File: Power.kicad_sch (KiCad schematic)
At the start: 74 parts, among them J100 CON-SOCJ-2155, Q100 T2N7002AK,LM, U100 LS1205EVD33, U101 SY8003ADFC, U102 SY8003ADFC, U103 SY8003ADFC, U104 SY8003ADFC, U105 BD3539FVM

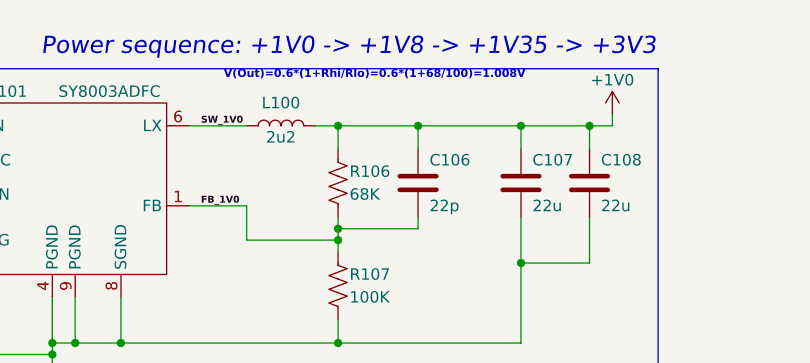
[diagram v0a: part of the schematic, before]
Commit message: Schematic page 2 done, Zynq Power
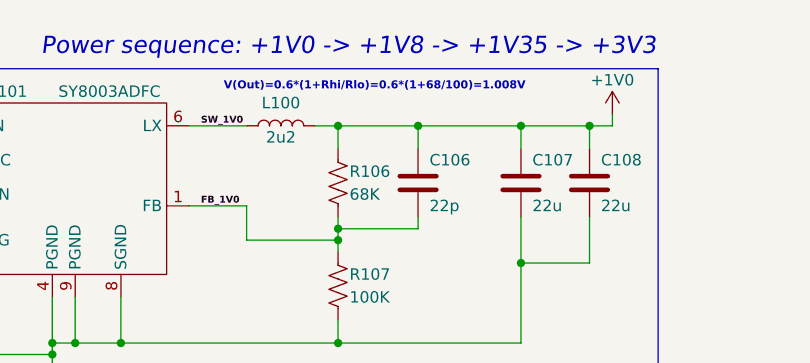
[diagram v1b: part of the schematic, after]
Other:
- title: ZeBra-X: A Xylinx Zynq Demo Board -> ZeBra-X: A Xilinx Zynq Demo Board
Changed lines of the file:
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@@
   (paper "A4")
   (title_block
-    (title "ZeBra-X: A Xylinx Zynq Demo Board")
+    (title "ZeBra-X: A Xilinx Zynq Demo Board")
     (date "2023-12-09")
     (rev "-")
@@
     (effects (font (size 1.27 1.27) bold) (justify left bottom))
   )
-  (text "V(Out)=0.6*(1+Rhi/Rlo)=0.6*(1+68/100)=1.008V" (at 234.95 20.32 0)
+  (text "V(Out)=0.6*(1+Rhi/Rlo)=0.6*(1+68/100)=1.008V" (at 234.95 21.59 0)
     (effects (font (size 0.889 0.889) bold) (justify left bottom))
   )

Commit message: Fixed Q100 footprint
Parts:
- Q100: footprint Package_TO_SOT_SMD:SOT-23 -> ZeBra_footprints:SOT23_TOS; symbol Simulation_SPICE:NMOS -> ZeBra-X:NMOS_T2N7002AKLM
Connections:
- net GND: now also Q100.2 (S); no longer Q100.3 (S)
- net LED_PWR_K: now also Q100.3 (D); no longer Q100.1 (D)
- net at R124.1: now also Q100.1 (G); no longer Q100.2 (G)
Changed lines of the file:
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@@
     )
   )
-  (symbol (lib_id "Simulation_SPICE:NMOS") (at 138.43 185.42 0) (unit 1)
+  (symbol (lib_id "ZeBra-X:NMOS_T2N7002AKLM") (at 138.43 185.42 0) (unit 1)
     (in_bom yes) (on_board yes) (dnp no)
     (property "Reference" "Q100" (at 132.08 189.23 0)
@@
       (effects (font (size 1.27 1.27)) (justify left))
     )
-    (property "Footprint" "Package_TO_SOT_SMD:SOT-23" (at 143.51 182.88 0)
+    (property "Footprint" "ZeBra_footprints:SOT23_TOS" (at 143.51 182.88 0)
       (effects (font (size 1.27 1.27)) hide)
     )

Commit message: Finished page 3 of schematic: Zynq Config, JTAG, Debug
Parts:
- R128: Distributor Link (none) -> -; LCSC PN (none) -> -; Manufacturer (none) -> -; Manufacturer PN (none) -> -
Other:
- title: ZeBra-X: A Xilinx Zynq Demo Board -> Power Supplies
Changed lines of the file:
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@@
   (paper "A4")
   (title_block
-    (title "ZeBra-X: A Xilinx Zynq Demo Board")
+    (title "Power Supplies")
     (date "2023-12-09")
     (rev "-")
@@
       (effects (font (size 1.27 1.27)) hide)
     )
-    (property "Datasheet" "" (at 35.56 176.53 0)
+    (property "Datasheet" "-" (at 35.56 176.53 0)
       (effects (font (size 1.27 1.27)) hide)
     )
-    (property "Description" "" (at 35.56 176.53 0)
+    (property "Description" "-" (at 35.56 176.53 0)
       (effects (font (size 1.27 1.27)) hide)
     )
-    (property "Distributor Link" "" (at 35.56 176.53 0)
+    (property "Distributor Link" "-" (at 35.56 176.53 0)
       (effects (font (size 1.27 1.27)) hide)
     )
-    (property "LCSC PN" "" (at 35.56 176.53 0)
+    (property "LCSC PN" "-" (at 35.56 176.53 0)
       (effects (font (size 1.27 1.27)) hide)
     )
-    (property "Manufacturer" "" (at 35.56 176.53 0)
+    (property "Manufacturer" "-" (at 35.56 176.53 0)
       (effects (font (size 1.27 1.27)) hide)
     )
-    (property "Manufacturer PN" "" (at 35.56 176.53 0)
+    (property "Manufacturer PN" "-" (at 35.56 176.53 0)
       (effects (font (size 1.27 1.27)) hide)
     )

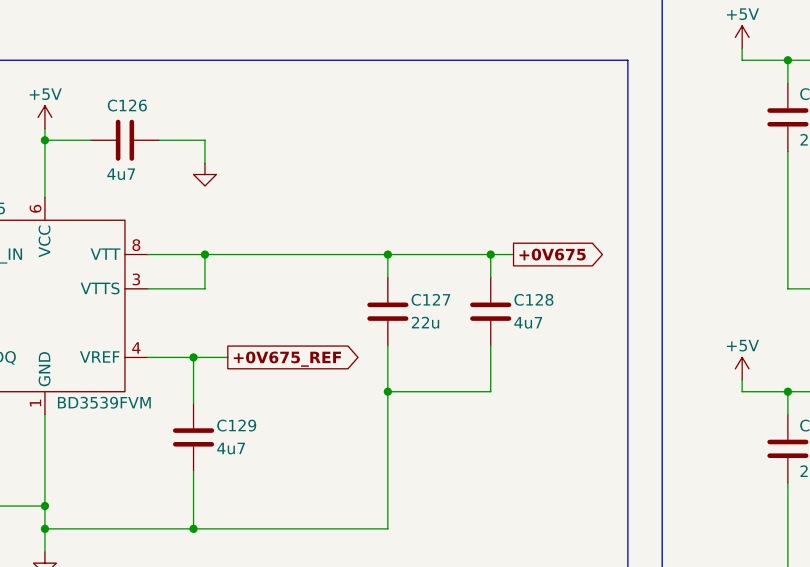
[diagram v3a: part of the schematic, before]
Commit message: Added page '[7] 1GB DDR3L Modules'
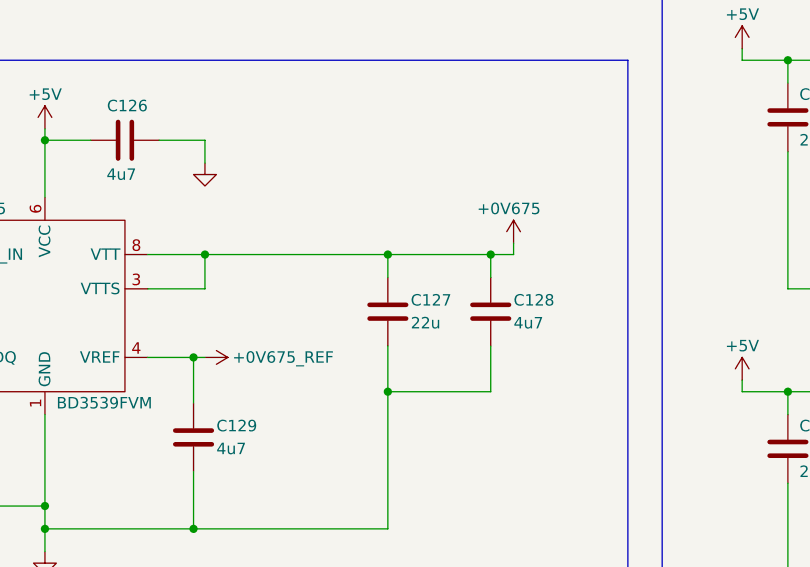
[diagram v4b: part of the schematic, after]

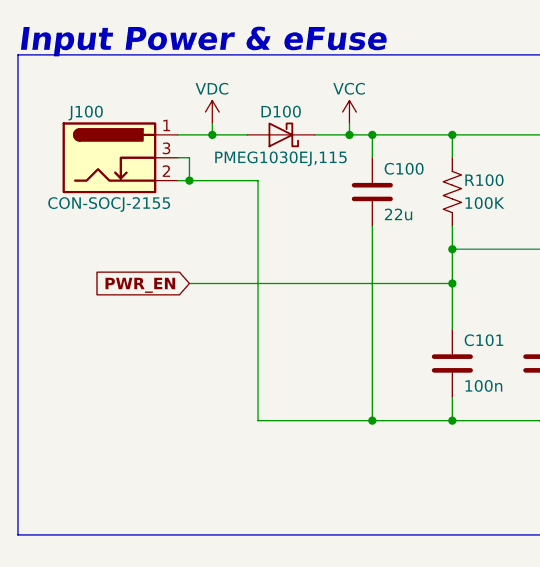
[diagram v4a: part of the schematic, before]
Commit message: Finished first pass of schematic, needs netclass assignments and double check
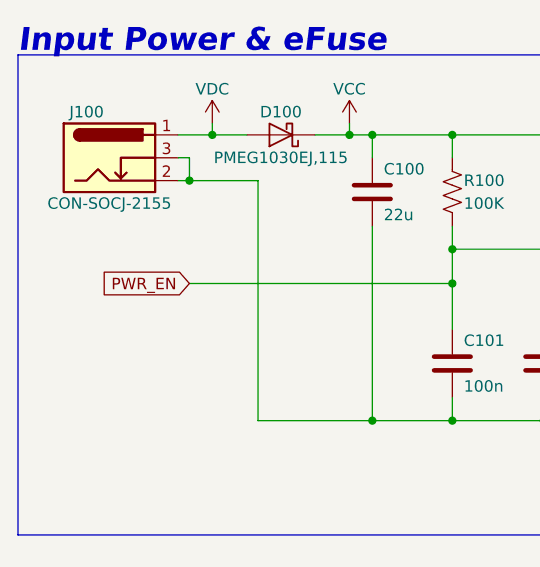
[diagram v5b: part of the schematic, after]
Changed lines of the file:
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@@
 			(font
 				(size 1.27 1.27)
-				(bold yes)
+				(thickness 0.1588)
 			)
 			(justify right)
